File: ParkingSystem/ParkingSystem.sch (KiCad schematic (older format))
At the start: 45 parts, among them J1 PJ-002A, J2 0430450400, J3 Conn_ARM_JTAG_SWD_10, J4 Conn_01x04_Female, J5 0430450200, Q1 SSM3K333R,LF, Q2 SSM3K333R,LF, Q3 SSM3K333R,LF, Q4 SSM3K333R,LF, Q5 SSM3K333R,LF, SW1 SW_Push, U1 R-78E5.0-1.0, U2 R-783.3-0.5, U3 STM32F103C4Tx, U4 DS1621S, Y1 Crystal

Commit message: Add few 3D Bodies, and more dimensions
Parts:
- H1, H2: symbol Mechanical:MountingHole -> ParkingSystem-rescue:MountingHole-Mechanical
- J2: footprint Connector_Molex:Molex_Micro-Fit_3.0_43045-0400_2x02_P3.00mm_Horizontal -> Connectors:Molex_Micro-Fit_3.0_43045-0400_2x02_P3.00mm_Horizontal
- J5: footprint Connector_Molex:Molex_Micro-Fit_3.0_43045-0200_2x01_P3.00mm_Horizontal -> Connectors:Molex_Micro-Fit_3.0_43045-0200_2x01_P3.00mm_Horizontal
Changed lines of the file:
@@
 F 0 "J2" H 2256 7075 50  0000 C CNN
 F 1 "0430450400" H 2256 6984 50  0000 C CNN
-F 2 "Connector_Molex:Molex_Micro-Fit_3.0_43045-0400_2x02_P3.00mm_Horizontal" H 2200 6650 50  0001 C CNN
+F 2 "Connectors:Molex_Micro-Fit_3.0_43045-0400_2x02_P3.00mm_Horizontal" H 2200 6650 50  0001 C CNN
 F 3 "" H 2200 6650 50  0001 C CNN
 	1    2200 6650
@@
 F 0 "J5" H 2256 7625 50  0000 C CNN
 F 1 "0430450200" H 2256 7534 50  0000 C CNN
-F 2 "Connector_Molex:Molex_Micro-Fit_3.0_43045-0200_2x01_P3.00mm_Horizontal" H 2200 7350 50  0001 C CNN
+F 2 "Connectors:Molex_Micro-Fit_3.0_43045-0200_2x01_P3.00mm_Horizontal" H 2200 7350 50  0001 C CNN
 F 3 "" H 2200 7350 50  0001 C CNN
 	1    2200 7350
@@
 NoConn ~ 7700 3100
 $Comp
-L Mechanical:MountingHole H2
+L ParkingSystem-rescue:MountingHole-Mechanical H2
 U 1 1 5C69771C
 P 5600 7400
@@
 $EndComp
 $Comp
-L Mechanical:MountingHole H1
+L ParkingSystem-rescue:MountingHole-Mechanical H1
 U 1 1 5C6978DE
 P 5600 7100

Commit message: Schematic outline
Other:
- note added: "Cortex\nDebug\nHeader"
- note added: "Power FETs"
- note added: "Power Regulation"
- note added: "Sensor/Indicator\nConnectors"
- note added: "Temp. Sensor"
- moved on the sheet: C15, H1, H2, J3, LS1, R10, R8, R9, U4

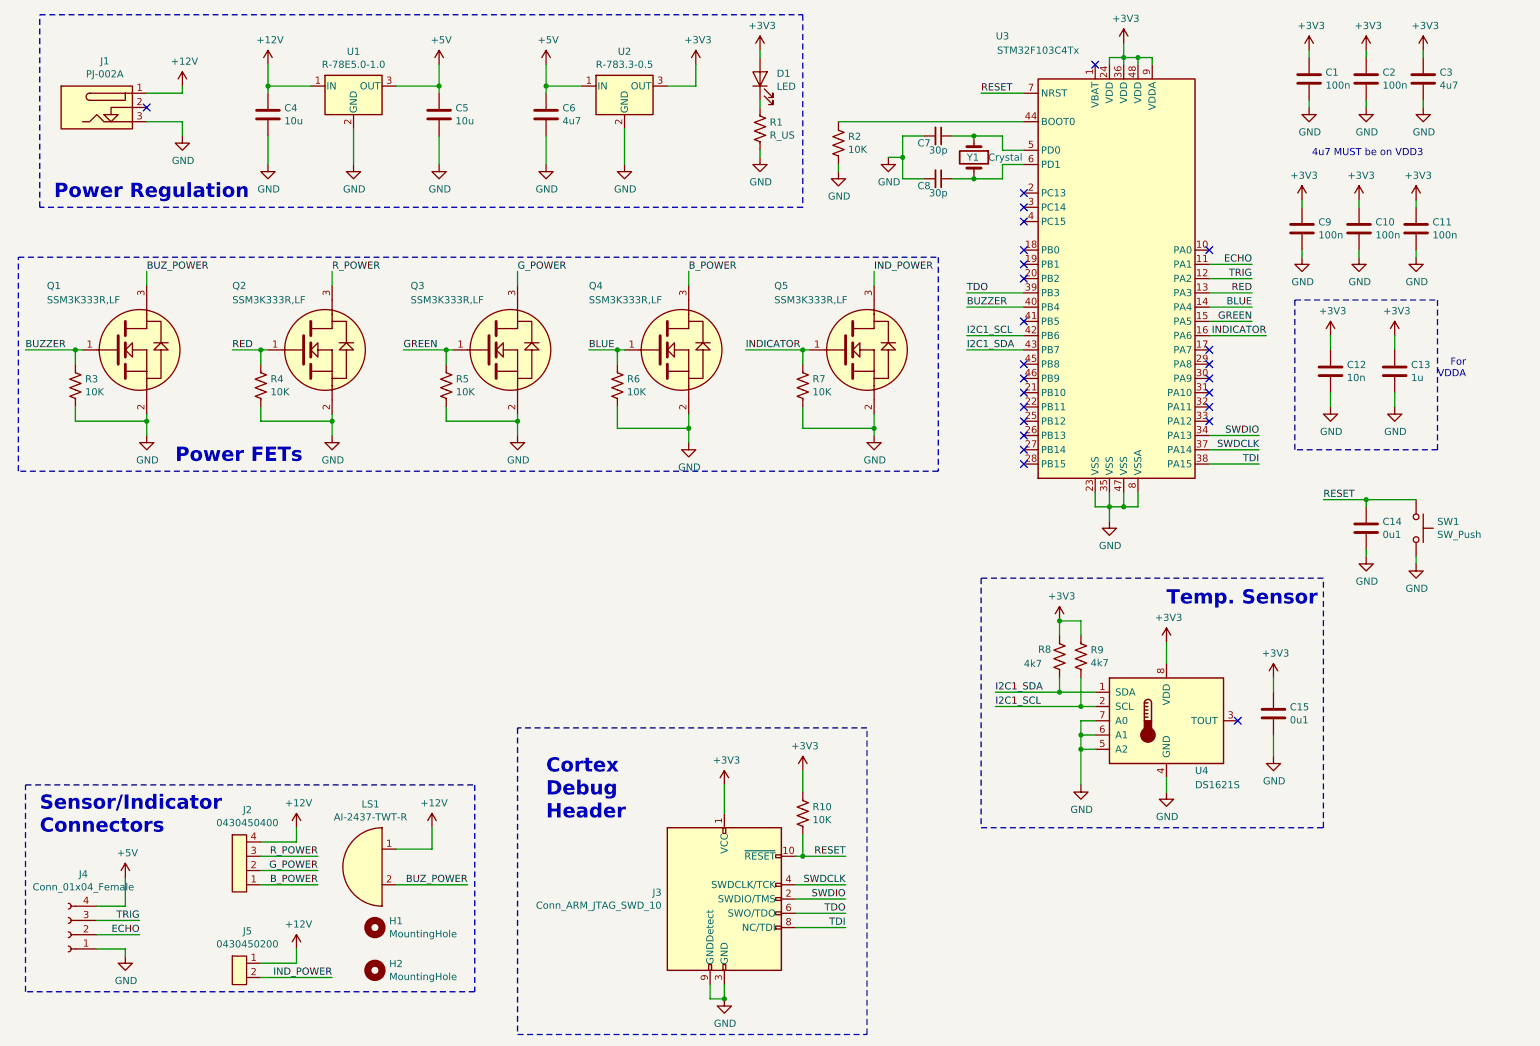
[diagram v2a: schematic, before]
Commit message: Add 7 Segment Drivers
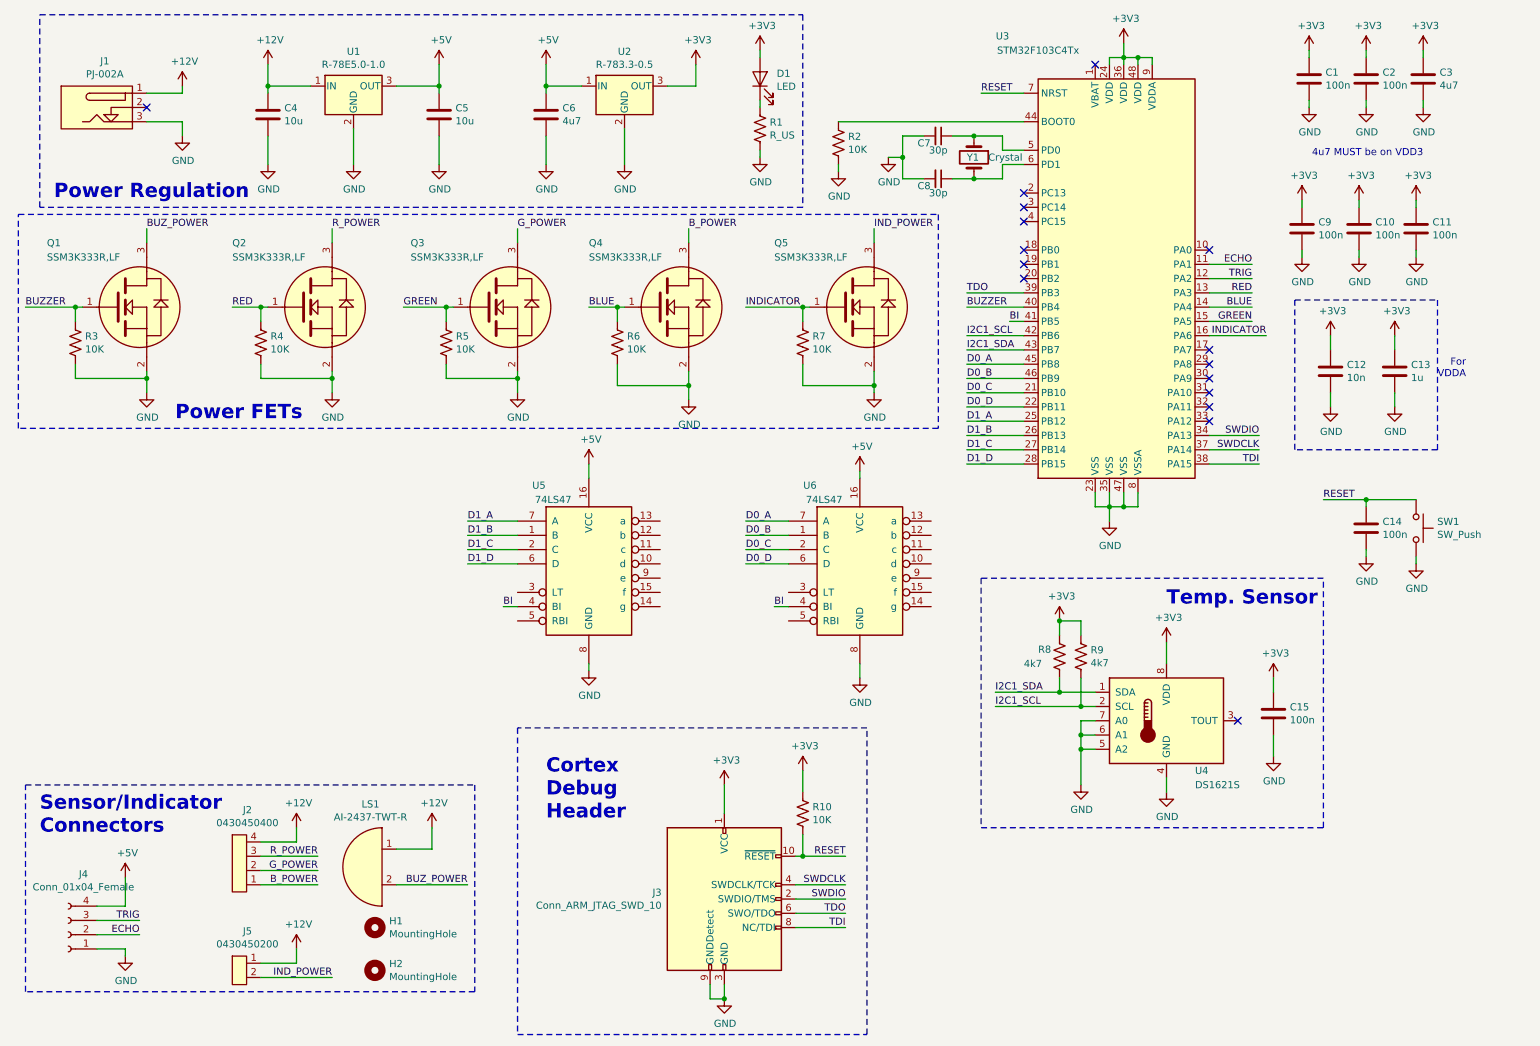
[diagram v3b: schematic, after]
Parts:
- added U5, U6: 74LS47, symbol 74xx:74LS47
- C14, C15: value 0u1 -> 100n
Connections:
- net +5V: now also U5.16 (VCC), U6.16 (VCC)
- net GND: now also U5.8 (GND), U6.8 (GND)
- net D0_C: now reaches U3.21 (PB10)
- net D0_C: now also U6.2 (C)
- net D0_D: now reaches U3.22 (PB11)
- net D0_D: now also U6.6 (D)
- net D1_A: now reaches U3.25 (PB12)
- net D1_A: now also U5.7 (A)
- net D1_B: now reaches U3.26 (PB13)
- net D1_B: now also U5.1 (B)
- net D1_C: now reaches U3.27 (PB14)
- net D1_C: now also U5.2 (C)
- net D1_D: now reaches U3.28 (PB15)
- net D1_D: now also U5.6 (D)
- net BI: now reaches U3.41 (PB5)
- net BI: now also U5.4 (BI), U6.4 (BI)
- net D0_A: now reaches U3.45 (PB8)
- net D0_A: now also U6.7 (A)
- net D0_B: now reaches U3.46 (PB9)
- net D0_B: now also U6.1 (B)
- no-connect marks 25 -> 16
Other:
- moved on the sheet: Q1, Q2, Q3, Q4, Q5, R3, R4, R5, R6, R7

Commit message: Add NMOS for 7 Seg
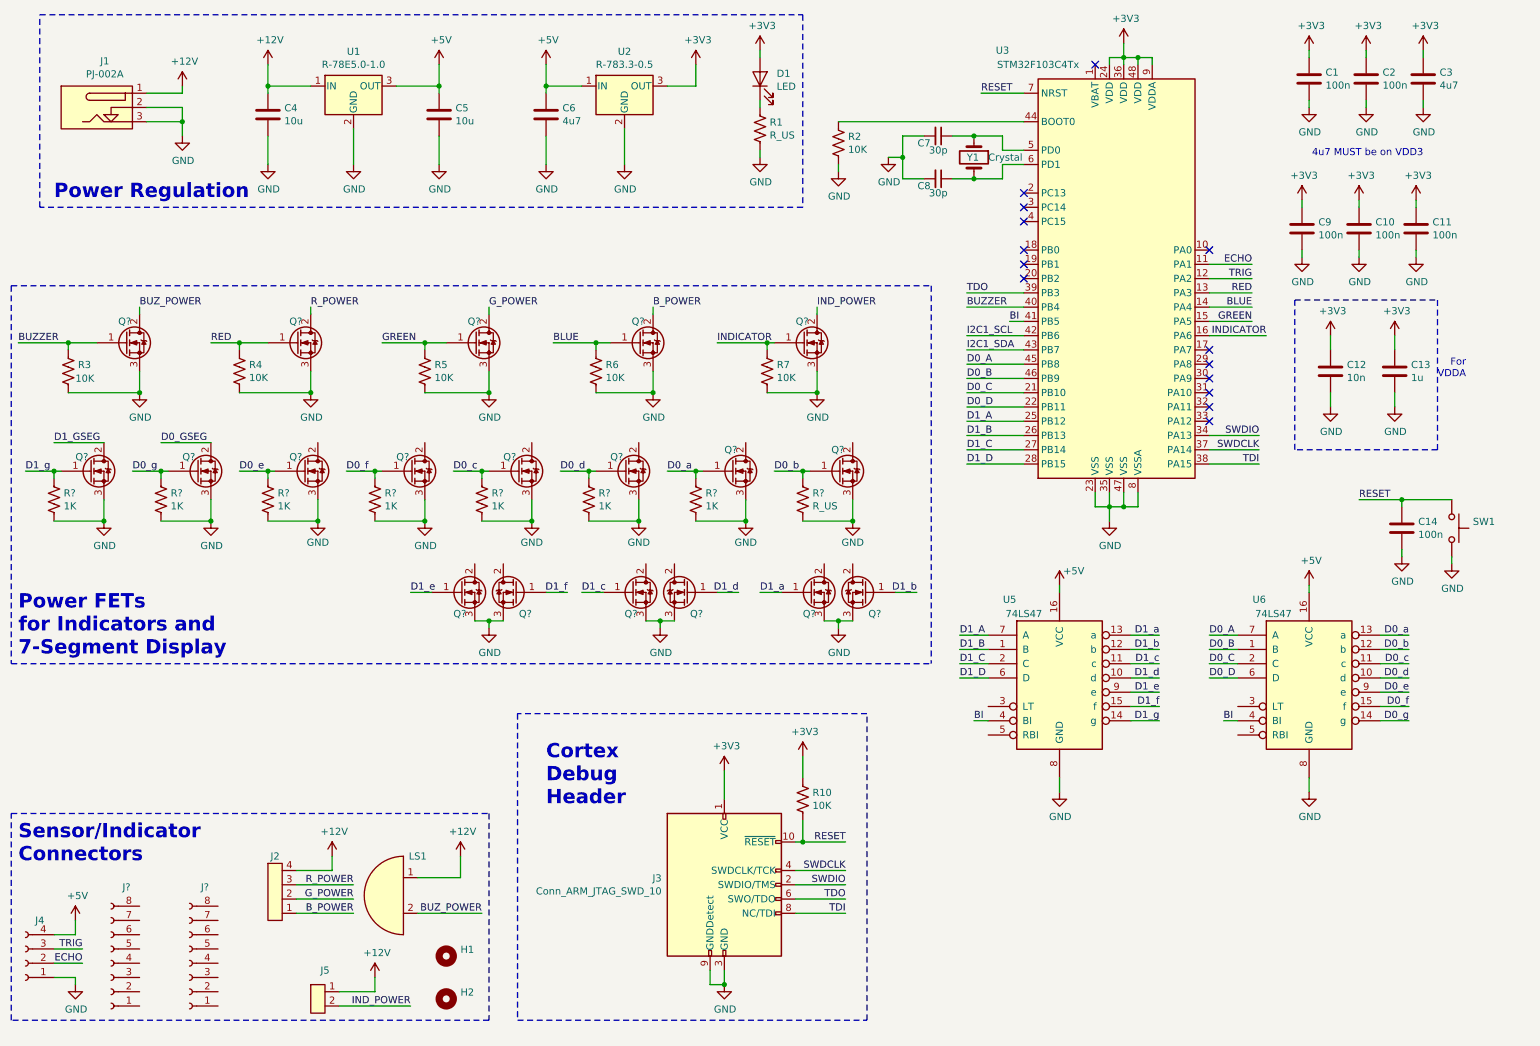
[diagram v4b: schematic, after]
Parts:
- removed C15: 100n, Capacitor_SMD:C_0603_1608Metric_Pad1.05x0.95mm_HandSolder, symbol ParkingSystem-rescue:C-Device
- removed Q1, Q2, Q3, Q4, Q5: SSM3K333R,LF, MOSFETS:SSM3K33R,LF, symbol ParkingSystem-rescue:SSM3K333R,LF-MOSFETS
- removed R8, R9: 4k7, Resistor_SMD:R_0603_1608Metric_Pad1.05x0.95mm_HandSolder, symbol ParkingSystem-rescue:R_US-Device
- removed U4: DS1621S, Package_SO:SOIC-8_3.9x4.9mm_P1.27mm, symbol ParkingSystem-rescue:DS1621S-Sensor_Temperature
- added J? (x2): Conn_01x08_Female, symbol Connector:Conn_01x08_Female
- added Q? (x17): Q_NMOS_GDS, symbol Device:Q_NMOS_GDS
- added Q? (x2): 1K, symbol Device:Q_NMOS_GDS
- added R? (x7): 1K, symbol Device:R_US
- added R?: R_US, symbol Device:R_US
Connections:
- net BLUE: now also Q?.1 (G)
- net BUZZER: now also Q?.1 (G)
- net BUZ_POWER: now also Q?.2 (D)
- net B_POWER: now also Q?.2 (D)
- net GND: now also J1.2, Q?.3 (S), Q?.3 (S), Q?.3 (S), Q?.3 (S), Q?.3 (S), Q?.3 (S), Q?.3 (S), Q?.3 (S), Q?.3 (S), Q?.3 (S), Q?.3 (S), Q?.3 (S), Q?.3 (S), Q?.3 (S), Q?.3 (S), Q?.3 (S), Q?.3 (S), Q?.3 (S), Q?.3 (S), R?.2, R?.2, R?.2, R?.2, R?.2, R?.2, R?.2, R?.2
- net GREEN: now also Q?.1 (G)
- net G_POWER: now also Q?.2 (D)
- net INDICATOR: now also Q?.1 (G)
- net IND_POWER: now also Q?.2 (D)
- net RED: now also Q?.1 (G)
- net R_POWER: now also Q?.2 (D)
- net D0_d: now reaches U6.10 (d)
- net D0_d: now also Q?.1 (G), R?.1
- net D0_c: now reaches U6.11 (c)
- net D0_c: now also Q?.1 (G), R?.1
- net D0_b: now reaches U6.12 (b)
- net D0_b: now also Q?.1 (G), R?.1
- net D0_a: now reaches U6.13 (a)
- net D0_a: now also Q?.1 (G), R?.1
- net D0_g: now reaches U6.14 (g)
- net D0_g: now also Q?.1 (G), R?.1
- net D0_f: now reaches U6.15 (f)
- net D0_f: now also Q?.1 (G), R?.1
- net D0_e: now reaches U6.9 (e)
- net D0_e: now also Q?.1 (G), R?.1
- net D1_d: now reaches U5.10 (d)
- net D1_d: now also Q?.1 (G)
- net D1_c: now reaches U5.11 (c)
- net D1_c: now also Q?.1 (G)
- net D1_b: now reaches U5.12 (b)
- net D1_b: now also Q?.1 (G)
- net D1_a: now reaches U5.13 (a)
- net D1_a: now also Q?.1 (G)
- net D1_g: now reaches U5.14 (g)
- net D1_g: now also Q?.1 (G), R?.1
- net D1_f: now reaches U5.15 (f)
- net D1_f: now also Q?.1 (G)
- net D1_e: now reaches U5.9 (e)
- net D1_e: now also Q?.1 (G)
- new net D0_GSEG: Q?.2 (D)
- new net D1_GSEG: Q?.2 (D)
- no-connect marks 16 -> 14
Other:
- note added: "Power FETs\nfor Indicators and\n7-Segment Display"
- note removed: "Power FETs"
- note removed: "Temp. Sensor"
- moved on the sheet: C14, H1, H2, J2, J3, J4, J5, LS1, R10, R3, R4, R5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

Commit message: Add 8-pin Molex for the 7-Seg
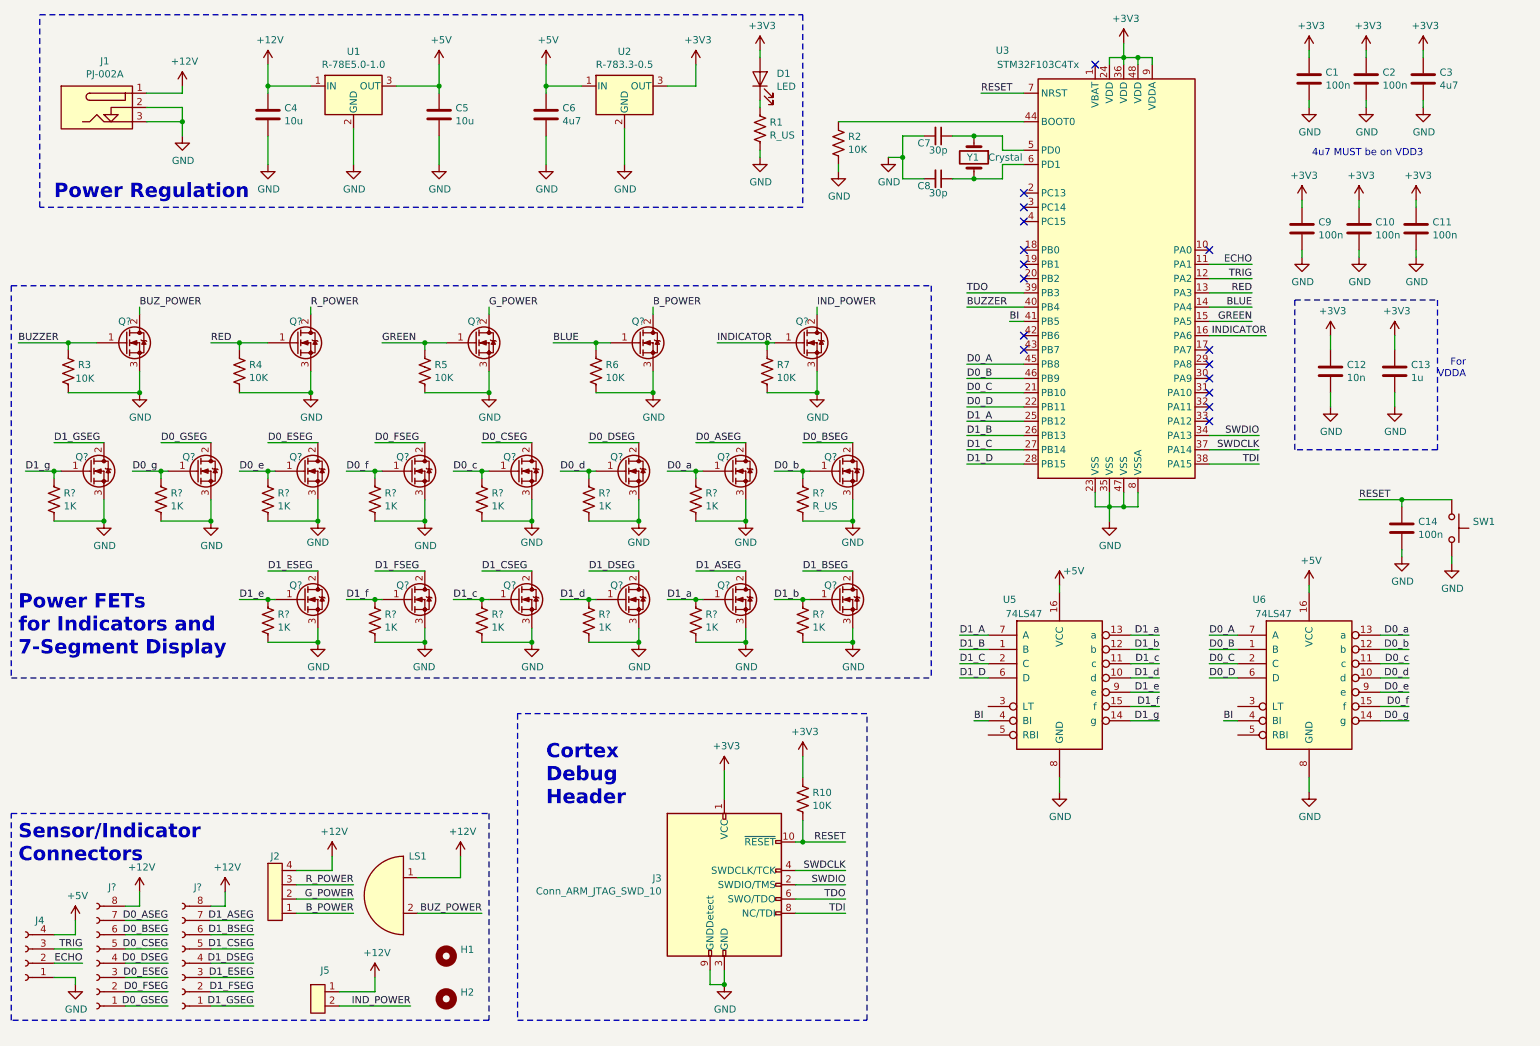
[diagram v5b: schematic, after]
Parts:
- added R? (x6): 1K, symbol Device:R_US
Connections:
- net +12V: now also J?.8 (Pin_8), J?.8 (Pin_8)
- net D0_GSEG: now also J?.1 (Pin_1)
- net D1_GSEG: now also J?.1 (Pin_1)
- net D1_a: now also R?.1
- net D1_b: now also R?.1
- net D1_c: now also R?.1
- net D1_d: now also R?.1
- net D1_e: now also R?.1
- net D1_f: now also R?.1
- net GND: now also R?.2, R?.2, R?.2, R?.2, R?.2, R?.2
- net D1_ASEG: now reaches Q?.2 (D)
- net D1_ASEG: now also J?.7 (Pin_7)
- net D1_CSEG: now reaches Q?.2 (D)
- net D1_CSEG: now also J?.5 (Pin_5)
- net D1_DSEG: now reaches Q?.2 (D)
- net D1_DSEG: now also J?.4 (Pin_4)
- net D1_FSEG: now reaches Q?.2 (D)
- net D1_FSEG: now also J?.2 (Pin_2)
- net D1_BSEG: now reaches Q?.2 (D)
- net D1_BSEG: now also J?.6 (Pin_6)
- net D1_ESEG: now reaches Q?.2 (D)
- net D1_ESEG: now also J?.3 (Pin_3)
- net D0_ASEG: now reaches Q?.2 (D)
- net D0_ASEG: now also J?.7 (Pin_7)
- net D0_CSEG: now reaches Q?.2 (D)
- net D0_CSEG: now also J?.5 (Pin_5)
- net D0_ESEG: now reaches Q?.2 (D)
- net D0_ESEG: now also J?.3 (Pin_3)
- net D0_BSEG: now reaches Q?.2 (D)
- net D0_BSEG: now also J?.6 (Pin_6)
- net D0_DSEG: now reaches Q?.2 (D)
- net D0_DSEG: now also J?.4 (Pin_4)
- net D0_FSEG: now reaches Q?.2 (D)
- net D0_FSEG: now also J?.2 (Pin_2)
- net I2C1_SCL: no longer names the net of U3.42 (PB6)
- net I2C1_SDA: no longer names the net of U3.43 (PB7)
- no-connect marks 14 -> 16
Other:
- moved on the sheet: J?, Q?
